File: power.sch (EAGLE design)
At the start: 34 parts, among them IC1 74HC125D, IC2 7805TV, IC3 7815TV

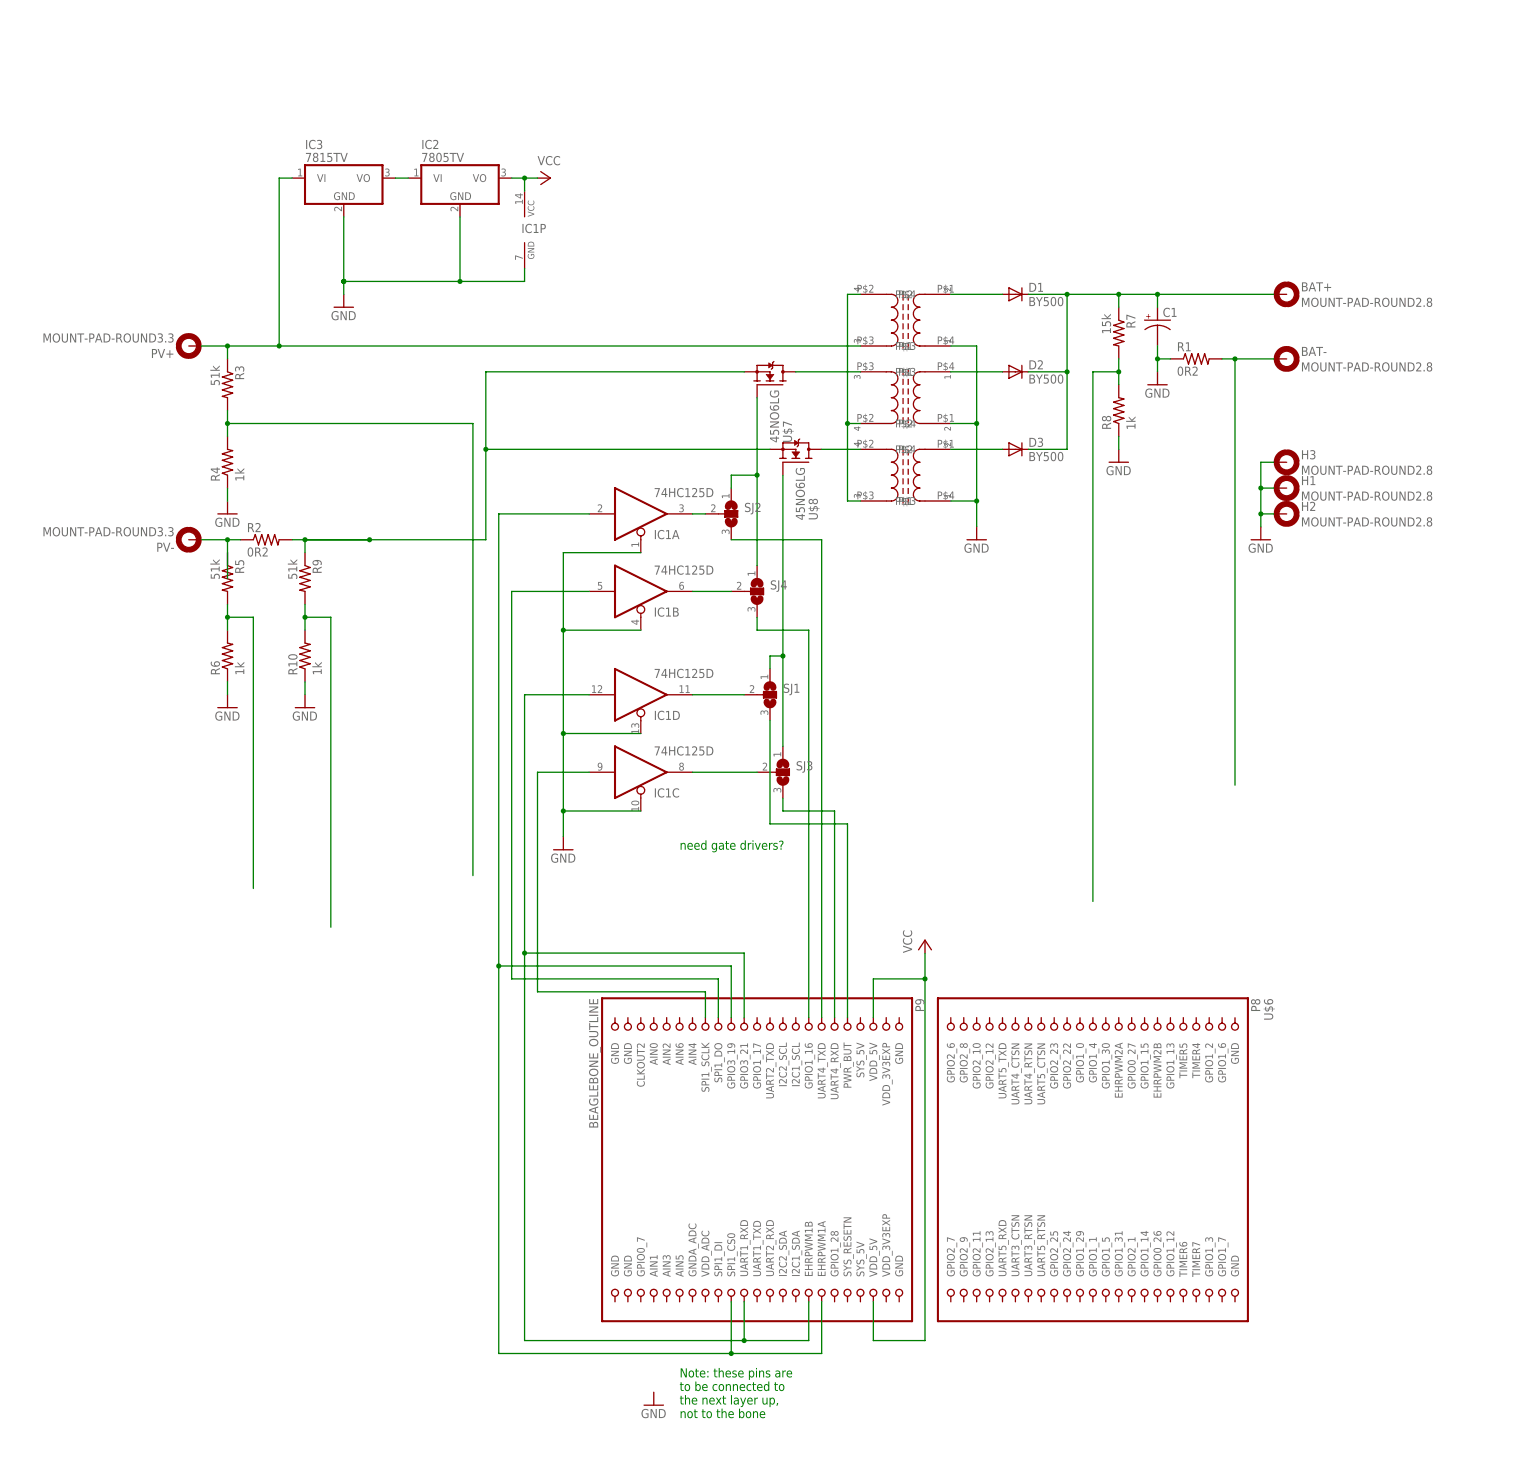
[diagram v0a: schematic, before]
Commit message: added LTC4151 I2C IV monotors to the schematic and some other fixes.  The prototype doesn't work yet, so watch out.
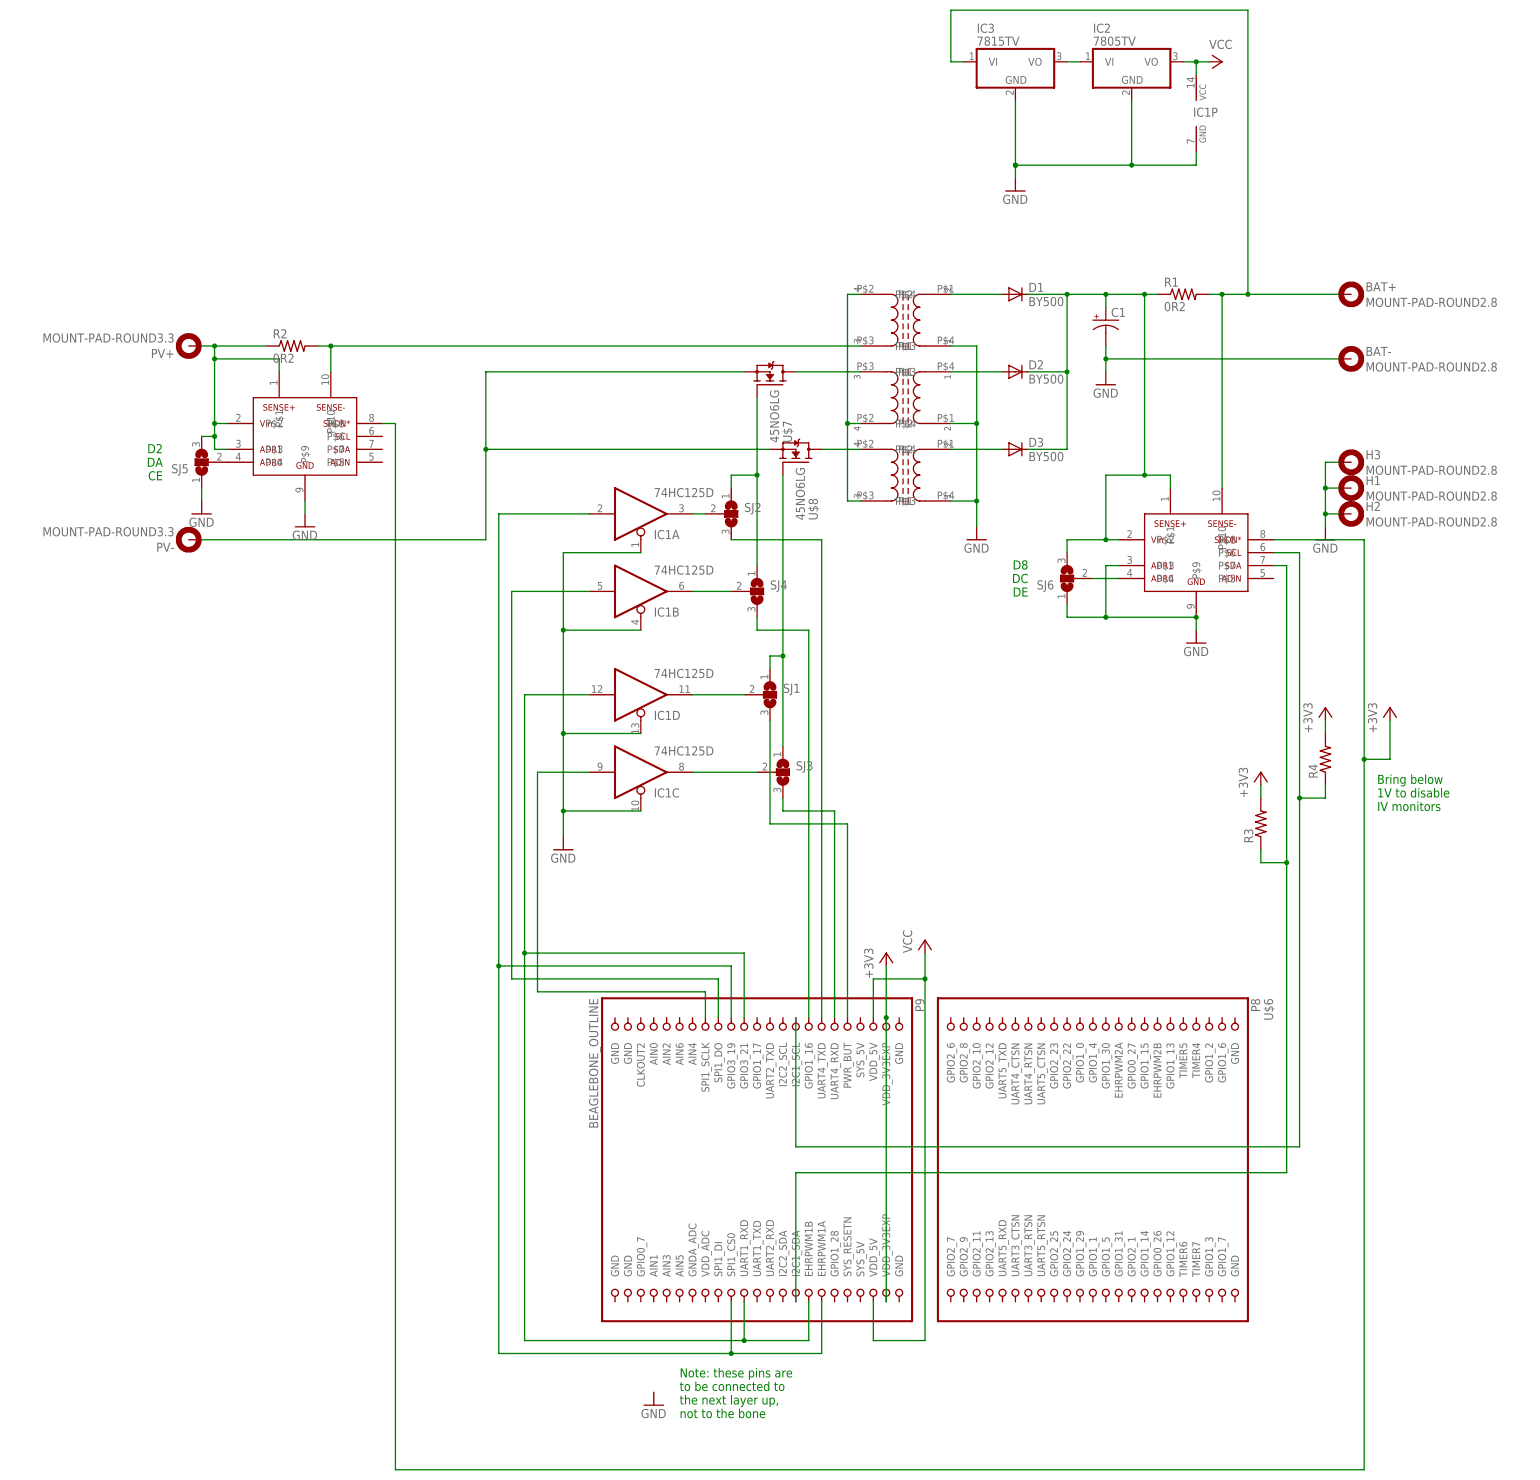
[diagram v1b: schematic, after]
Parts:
- removed R10, R6, R8: 1k, rcl:R-US_R0603
- removed R5, R9: 51k, rcl:R-US_R0603
- removed R7: 15k, rcl:R-US_R0603
- added SJ5, SJ6: (no value), jumper:SJ2W
- added U$1, U$2: LTC4151, semiconductors:LTC4151
- R3: value 51k -> (none)
- R4: value 1k -> (none)
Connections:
- removed net N$17: R5.2, R6.2
- removed net N$18: R10.2, R9.2
- new net +3V3: R3.2, R4.2, U$1.P$8, U$2.P$8, U$6.VDD_3V3EXP@1, U$6.VDD_3V3EXP@2
- new net N$14: R4.1, U$2.P$6, U$6.I2C1_SCL
- new net N$26: SJ6.2, U$2.P$4
- net GND: now also BAT-.MOUNT, SJ5.1, SJ6.1, U$1.P$9, U$2.P$3, U$2.P$9; no longer R1.1, R10.1, R4.1, R6.1, R8.1
- net N$10: now also SJ5.2, U$1.P$4; no longer R7.2, R8.2
- net N$12: now also C1.+, D1.C, D2.C, D3.C, R1.1, SJ6.3, U$2.P$1, U$2.P$2; no longer R3.2, R4.2
- net N$16: now also PV+.MOUNT, SJ5.3, U$1.P$1, U$1.P$2, U$1.P$3; no longer PV-.MOUNT, R5.1
- net N$4: now also BAT+.MOUNT, IC3.VI, U$2.P$10; no longer BAT-.MOUNT
- net N$6: now also R2.2, U$1.P$10; no longer IC3.VI, PV+.MOUNT, R3.1
- net N$7: now also R3.1, U$2.P$7, U$6.I2C1_SDA; no longer BAT+.MOUNT, C1.+, D1.C, D2.C, D3.C, R7.1
- net N$8: now also PV-.MOUNT; no longer R2.2, R9.1
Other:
- note added: "Bring below 1V to disable IV monitors"
- note added: "D2 DA CE"
- note added: "D8 DC DE"
- note removed: "need gate drivers?"
- moved on the sheet: BAT+, BAT-, C1, H1, H2, H3, IC1P, IC2, IC3, R1, R2, R3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

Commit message: whomp
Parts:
- removed IC1: 74HC125D, 74xx-eu:74HC125D
- removed IC3: 7815TV, linear:7815TV
- removed SJ1, SJ2, SJ3, SJ4: (no value), jumper:SJ2W
- added R10, R11, R12, R13, R14, R15, R16, R17, R18, R19, R20, R21, R22, R23, R24, R25, R26, R27, R28, R29, R30, R7, R8, R9: 0, rcl:R-US_R0603
- added R5, R6: 10k, rcl:R-US_R0603
- U$7, U$8: value 45NO6LG -> SIA446DJ; device semiconductors:45NO6LG -> semiconductors:SIA446DJ
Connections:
- removed net N$27: IC2.VI, IC3.VO
- new net N$17: R9.1, U$6.SPI1_SCLK
- new net N$18: R10.1, U$6.SPI1_DI
- new net N$30: R5.2, R6.1, U$1.P$5
- new net N$31: R26.1, U$6.GPIO2_8
- new net N$32: R27.1, U$6.GPIO2_11
- new net N$34: R29.1, U$6.GPIO2_13
- new net N$35: R30.1, U$6.GPIO2_12
- new net N$36: U$6.GPIO1_12
- new net N$39: R19.1, U$6.GPIO1_30
- new net N$40: R18.1, U$6.GPIO2_22
- new net N$41: R17.1, U$6.GPIO2_24
- new net N$42: R16.1, U$6.GPIO2_23
- new net N$43: U$6.GPIO2_25
- new net N$44: R10.2, R12.2, R14.2, R16.2, R18.2, R20.2, R22.2, R24.2, R26.2, R28.2, R30.2, R8.2, U$7.G
- new net N$45: R11.2, R13.2, R15.2, R17.2, R19.2, R21.2, R23.2, R25.2, R27.2, R29.2, R7.2, R9.2, U$8.G
- net GND: now also R6.2, U$6.GND@2; no longer IC1A.OE, IC1B.OE, IC1C.OE, IC1D.OE, IC1P.GND, IC3.GND
- net N$11: now also R15.1; no longer SJ1.1, SJ3.1, U$8.G
- net N$13: now also R21.1; no longer SJ2.1, SJ4.1, U$7.G
- net N$14: now also U$1.P$6, U$6.UART1_TXD; no longer U$6.I2C1_SCL
- net N$19: now also R11.1, U$6.SPI1_DO; no longer SJ1.3, U$6.PWR_BUT
- net N$20: now also R7.1, U$6.CLKOUT2; no longer IC1A.O, SJ2.2
- net N$21: now also R8.1, U$6.GPIO0_7; no longer SJ3.3, U$6.UART4_RXD
- net N$22: now also R12.1, U$6.SPI1_CS0; no longer SJ4.3, U$6.GPIO1_16
- net N$23: now also R13.1; no longer IC1A.I, U$6.EHRPWM1A, U$6.SPI1_CS0
- net N$24: now also R14.1, U$6.GPIO3_21; no longer IC1B.O, SJ4.2
- net N$25: now also R23.1, U$6.GPIO2_7; no longer IC1D.O, SJ1.2
- net N$28: now also R24.1, U$6.GPIO2_6; no longer IC1D.I, U$6.EHRPWM1B, U$6.GPIO3_21, U$6.UART1_RXD
- net N$29: now also R25.1, U$6.GPIO2_9; no longer IC1C.O, SJ3.2
- net N$33: now also R28.1, U$6.GPIO2_10; no longer SJ2.3, U$6.UART4_TXD
- net N$37: now also R22.1, U$6.GPIO1_13; no longer IC1B.I, U$6.SPI1_DO
- net N$38: now also R20.1, U$6.GPIO1_31; no longer IC1C.I, U$6.SPI1_SCLK
- net N$4: now also IC2.VI; no longer IC3.VI
- net N$7: now also U$1.P$7, U$6.UART1_RXD; no longer U$6.I2C1_SDA
- net N$8: now also R5.1
- net VCC: no longer IC1P.VCC
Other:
- note added: "leave r6 out if this line stays between 0 and 2.048V"
- note removed: "Note: these pins are to be connected to the next layer up, not to the bone"
- moved on the sheet: U$6

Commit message: don't worry, it's not as bad as it looks
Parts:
- R3, R4: value (none) -> 47k
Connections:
- removed net N$36: U$6.GPIO1_12
- removed net N$43: U$6.GPIO2_25
- net N$11: now also U$6.GPIO2_25
- net N$13: now also U$6.GPIO1_12
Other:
- note added: "programming jumpers: pick two"
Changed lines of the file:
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@@
 <part name="+3V1" library="supply1" deviceset="+3V3" device=""/>
 <part name="+3V2" library="supply1" deviceset="+3V3" device=""/>
-<part name="R3" library="rcl" deviceset="R-US_" device="R0603"/>
+<part name="R3" library="rcl" deviceset="R-US_" device="R0603" value="47k"/>
 <part name="+3V3" library="supply1" deviceset="+3V3" device=""/>
-<part name="R4" library="rcl" deviceset="R-US_" device="R0603"/>
+<part name="R4" library="rcl" deviceset="R-US_" device="R0603" value="47k"/>
 <part name="GND4" library="supply1" deviceset="GND" device=""/>
 <part name="+3V4" library="supply1" deviceset="+3V3" device=""/>
@@
 this line stays
 between 0 and 2.048V</text>
+<text x="-20.32" y="38.1" size="1.778" layer="91">programming jumpers:
+pick two</text>
 </plain>
 <instances>
@@
 <segment>
 <pinref part="U$8" gate="G$1" pin="S"/>
-<wire x1="-15.24" y1="58.42" x2="-15.24" y2="76.2" width="0.1524" layer="91"/>
-<wire x1="40.64" y1="76.2" x2="-15.24" y2="76.2" width="0.1524" layer="91"/>
+<wire x1="25.4" y1="58.42" x2="25.4" y2="76.2" width="0.1524" layer="91"/>
+<wire x1="40.64" y1="76.2" x2="25.4" y2="76.2" width="0.1524" layer="91"/>
 <pinref part="U$7" gate="G$1" pin="S"/>
-<wire x1="35.56" y1="91.44" x2="-15.24" y2="91.44" width="0.1524" layer="91"/>
-<wire x1="-15.24" y1="91.44" x2="-15.24" y2="76.2" width="0.1524" layer="91"/>
-<junction x="-15.24" y="76.2"/>
+<wire x1="35.56" y1="91.44" x2="25.4" y2="91.44" width="0.1524" layer="91"/>
+<wire x1="25.4" y1="91.44" x2="25.4" y2="76.2" width="0.1524" layer="91"/>
+<junction x="25.4" y="76.2"/>
 <pinref part="PV-" gate="G$1" pin="MOUNT"/>
 <wire x1="-71.12" y1="58.42" x2="-22.86" y2="58.42" width="0.1524" layer="91"/>
 <pinref part="R5" gate="G$1" pin="1"/>
-<wire x1="-22.86" y1="58.42" x2="-15.24" y2="58.42" width="0.1524" layer="91"/>
+<wire x1="-22.86" y1="58.42" x2="25.4" y2="58.42" width="0.1524" layer="91"/>
 <wire x1="-22.86" y1="60.96" x2="-22.86" y2="58.42" width="0.1524" layer="91"/>
 <junction x="-22.86" y="58.42"/>
@@
 </segment>
 </net>
-<net name="N$36" class="0">
-<segment>
-<pinref part="U$6" gate="G$1" pin="GPIO1_12"/>
-<wire x1="-10.16" y1="-91.44" x2="-10.16" y2="-92.71" width="0.1524" layer="91"/>
-<wire x1="-10.16" y1="-92.71" x2="-8.89" y2="-92.71" width="0.1524" layer="91"/>
-<wire x1="-8.89" y1="-92.71" x2="-8.89" y2="-21.59" width="0.1524" layer="91"/>
-</segment>
-</net>
 <net name="N$37" class="0">
 <segment>
@@
 <pinref part="R16" gate="G$1" pin="1"/>
 <wire x1="22.86" y1="2.54" x2="22.86" y2="43.18" width="0.1524" layer="91"/>
-</segment>
-</net>
-<net name="N$43" class="0">
-<segment>
-<pinref part="U$6" gate="G$1" pin="GPIO2_25"/>
-<wire x1="12.7" y1="-91.44" x2="12.7" y2="-92.71" width="0.1524" layer="91"/>
-<wire x1="12.7" y1="-92.71" x2="13.97" y2="-92.71" width="0.1524" layer="91"/>
-<wire x1="13.97" y1="-92.71" x2="13.97" y2="-21.59" width="0.1524" layer="91"/>
 </segment>
 </net>
@@
 <net name="N$11" class="0">
 <segment>
-<wire x1="13.97" y1="-21.59" x2="13.97" y2="0" width="0.1524" layer="91"/>
 <wire x1="13.97" y1="0" x2="25.4" y2="0" width="0.1524" layer="91"/>
 <pinref part="R15" gate="G$1" pin="1"/>
 <wire x1="25.4" y1="0" x2="25.4" y2="27.94" width="0.1524" layer="91"/>
+<pinref part="U$6" gate="G$1" pin="GPIO2_25"/>
+<wire x1="12.7" y1="-91.44" x2="12.7" y2="-92.71" width="0.1524" layer="91"/>
+<wire x1="12.7" y1="-92.71" x2="13.97" y2="-92.71" width="0.1524" layer="91"/>
+<wire x1="13.97" y1="-92.71" x2="13.97" y2="0" width="0.1524" layer="91"/>
 </segment>
 </net>
 <net name="N$13" class="0">
 <segment>
-<wire x1="-8.89" y1="-21.59" x2="-8.89" y2="15.24" width="0.1524" layer="91"/>
 <wire x1="-8.89" y1="15.24" x2="10.16" y2="15.24" width="0.1524" layer="91"/>
 <pinref part="R21" gate="G$1" pin="1"/>
 <wire x1="10.16" y1="15.24" x2="10.16" y2="27.94" width="0.1524" layer="91"/>
-</segment>
-</net>
+<pinref part="U$6" gate="G$1" pin="GPIO1_12"/>
+<wire x1="-10.16" y1="-91.44" x2="-10.16" y2="-92.71" width="0.1524" layer="91"/>
+<wire x1="-10.16" y1="-92.71" x2="-8.89" y2="-92.71" width="0.1524" layer="91"/>
+<wire x1="-8.89" y1="-92.71" x2="-8.89" y2="15.24" width="0.1524" layer="91"/>
+</segment>
+</net>

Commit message: still working on it
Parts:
- added C2: 100pf, rcl:C-USC0603K
- R5, R6: value 10k -> 12k
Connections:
- net GND: now also C2.1
- net N$30: now also C2.2
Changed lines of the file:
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@@
 <part name="SJ5" library="jumper" deviceset="SJ2W" device=""/>
 <part name="SJ6" library="jumper" deviceset="SJ2W" device=""/>
-<part name="R5" library="rcl" deviceset="R-US_" device="R0603" value="10k"/>
-<part name="R6" library="rcl" deviceset="R-US_" device="R0603" value="10k"/>
+<part name="R5" library="rcl" deviceset="R-US_" device="R0603" value="12k"/>
+<part name="R6" library="rcl" deviceset="R-US_" device="R0603" value="12k"/>
 <part name="GND5" library="supply1" deviceset="GND" device=""/>
 <part name="R7" library="rcl" deviceset="R-US_" device="R0603" value="0"/>
@@
 <part name="R29" library="rcl" deviceset="R-US_" device="R0603" value="0"/>
 <part name="R30" library="rcl" deviceset="R-US_" device="R0603" value="0"/>
+<part name="C2" library="rcl" deviceset="C-US" device="C0603K" value="100pf"/>
 </parts>
 <sheets>
@@
 <instance part="R29" gate="G$1" x="33.02" y="33.02" rot="R90"/>
 <instance part="R30" gate="G$1" x="30.48" y="48.26" rot="R90"/>
+<instance part="C2" gate="G$1" x="-25.4" y="83.82"/>
 </instances>
 <busses>
@@
 <wire x1="-22.86" y1="91.44" x2="-17.78" y2="91.44" width="0.1524" layer="91"/>
 <wire x1="-17.78" y1="91.44" x2="-17.78" y2="86.36" width="0.1524" layer="91"/>
+<pinref part="C2" gate="G$1" pin="1"/>
+<wire x1="-25.4" y1="86.36" x2="-25.4" y2="91.44" width="0.1524" layer="91"/>
+<wire x1="-25.4" y1="91.44" x2="-22.86" y2="91.44" width="0.1524" layer="91"/>
+<junction x="-22.86" y="91.44"/>
 </segment>
 <segment>
@@
 <pinref part="U$1" gate="G$1" pin="P$5"/>
 <pinref part="R6" gate="G$1" pin="1"/>
-<wire x1="-35.56" y1="73.66" x2="-22.86" y2="73.66" width="0.1524" layer="91"/>
+<wire x1="-35.56" y1="73.66" x2="-25.4" y2="73.66" width="0.1524" layer="91"/>
+<wire x1="-25.4" y1="73.66" x2="-22.86" y2="73.66" width="0.1524" layer="91"/>
 <wire x1="-22.86" y1="73.66" x2="-22.86" y2="76.2" width="0.1524" layer="91"/>
 <pinref part="R5" gate="G$1" pin="2"/>
 <wire x1="-22.86" y1="73.66" x2="-22.86" y2="71.12" width="0.1524" layer="91"/>
 <junction x="-22.86" y="73.66"/>
-</segment>
-</net>
+<pinref part="C2" gate="G$1" pin="2"/>
+<wire x1="-25.4" y1="78.74" x2="-25.4" y2="73.66" width="0.1524" layer="91"/>
+<junction x="-25.4" y="73.66"/>
+</segment>
+</net>
